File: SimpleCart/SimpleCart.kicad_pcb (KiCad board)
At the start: 2 copper layers, 90 x 56.8 mm, 9 parts, among them J1 CommanderX16Expansion Alt, U1 SST39SF040 (ROM), U2 74HCT00, U3 74HCT138

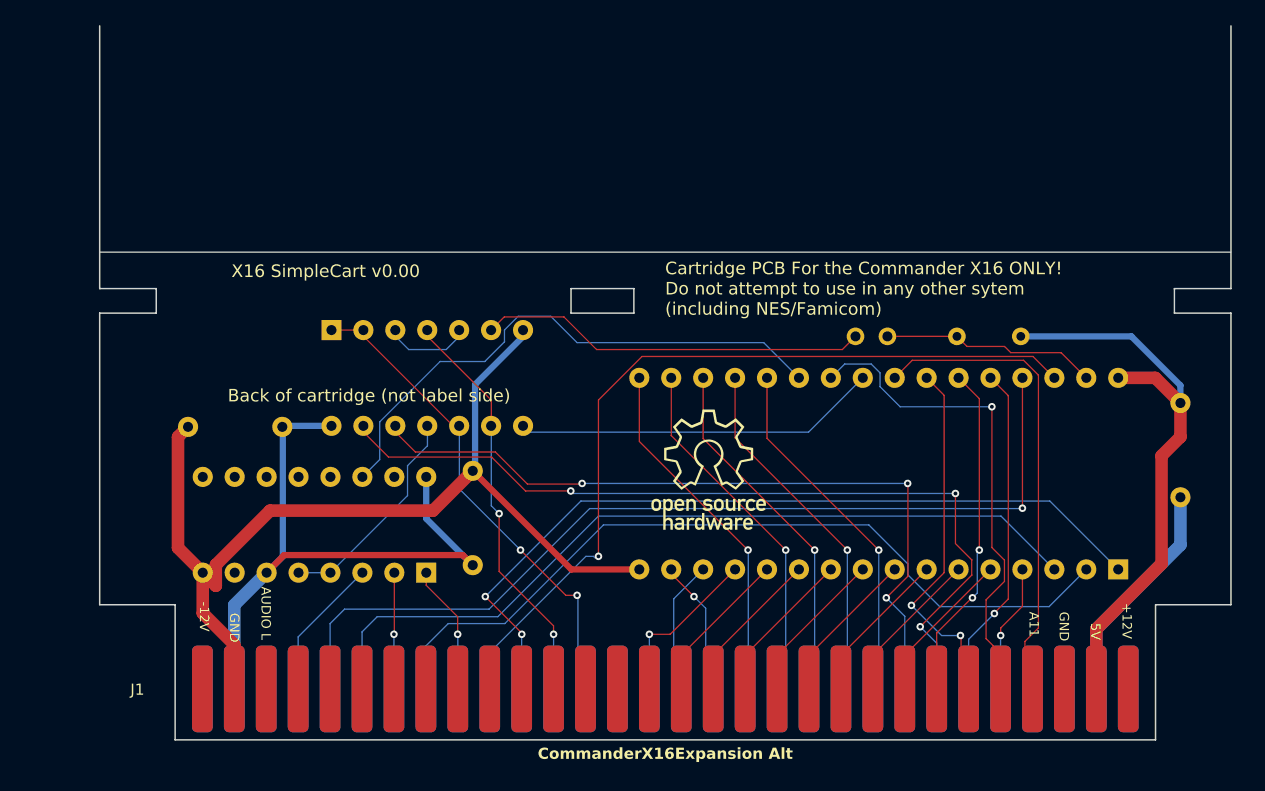
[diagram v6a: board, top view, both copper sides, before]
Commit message: Tweaks to both Simplecart and ROAM
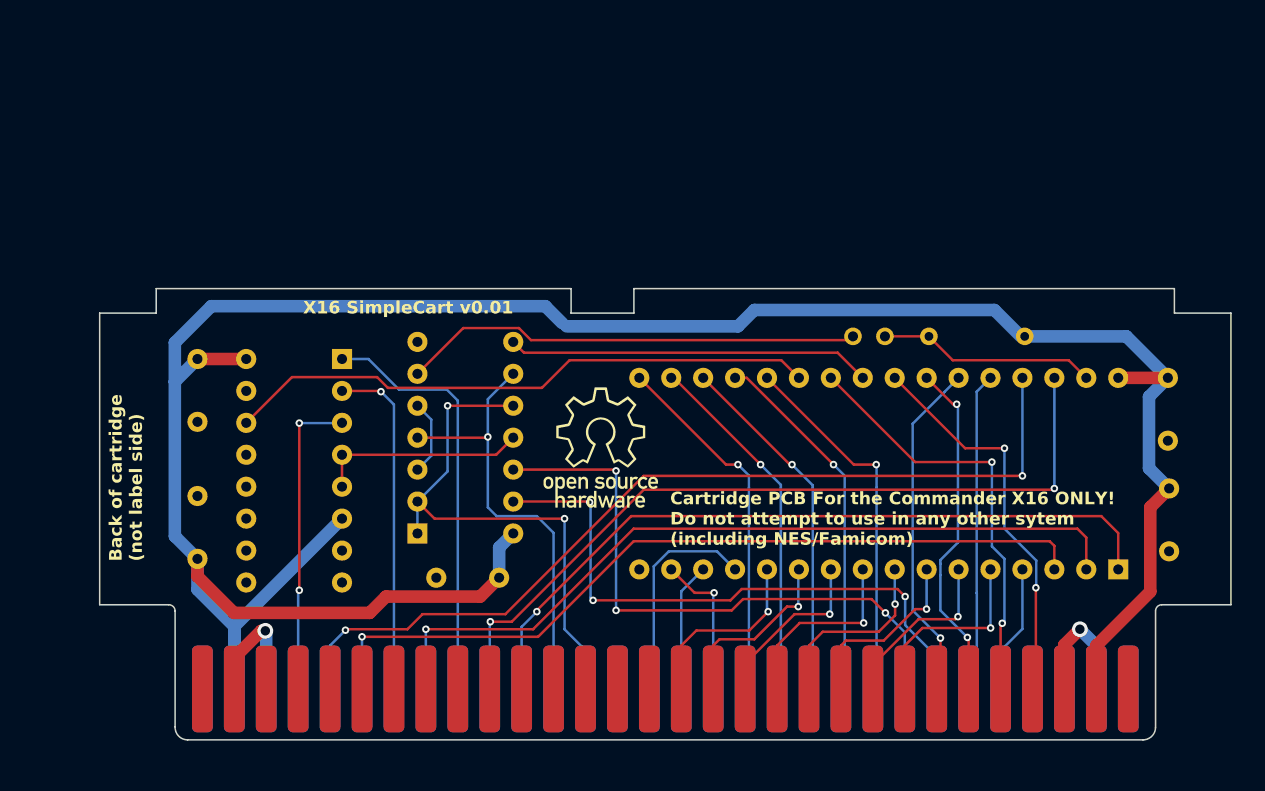
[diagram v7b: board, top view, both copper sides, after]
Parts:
- added C4: 1uF, Capacitor_THT:C_Disc_D4.3mm_W1.9mm_P5.00mm, B.Cu at (133.1, 119.8)
- added C5: 1uF, Capacitor_THT:C_Disc_D4.3mm_W1.9mm_P5.00mm, B.Cu at (55.8, 115.4)
- C1, C2, C3: footprint Capacitor_THT:C_Axial_L3.8mm_D2.6mm_P7.50mm_Horizontal -> Capacitor_THT:C_Disc_D4.3mm_W1.9mm_P5.00mm
- J1: footprint CommanderX16Expansion:CommanderX16Cartridge -> CommanderX16Expansion:CommanderX16SimpleCartridge
- JP1: value WRITE ENABLE -> WRITE EN
- R1: footprint Resistor_THT:R_Axial_DIN0204_L3.6mm_D1.6mm_P5.08mm_Horizontal -> Resistor_THT:R_Axial_DIN0204_L3.6mm_D1.6mm_P7.62mm_Horizontal
- moved U3 18.3 mm to (67.3, 104.5), turned to 180 degrees
- moved U2 17.6 mm to (73.3, 118.4), turned to 0 degrees
- moved C2 8.98 mm to (74.8, 121.9), turned to 0 degrees
- moved C3 8.64 mm to (55.8, 104.5), turned to -90 degrees
- moved C1 4.61 mm to (133.0, 111.0)
- moved R1 2.23 mm to (114.0, 102.7)
- moved JP1 0.20 mm to (108.0, 102.7)
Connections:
- J1 pad 1: Net-(J1--12V-Pad1) -> unconnected-(J1--12V-Pad1)_1
- J1 pad 2: Net-(J1-+12V-Pad2) -> unconnected-(J1-+12V-Pad2)
- J1 pad 59: Net-(J1-+12V-Pad2) -> unconnected-(J1-+12V-Pad2)_1
- J1 pad 60: Net-(J1--12V-Pad1) -> unconnected-(J1--12V-Pad1)
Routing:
- net +5V: track 99.0 -> 200.1 mm
- net GND: track 96.6 -> 21.0 mm, vias 0 -> 2
- net Net-(J1-ROMB5): track 12.9 -> 33.5 mm, vias 1 -> 0
- net Net-(J1-A14): track 67.6 -> 47.9 mm
- net Net-(J1-ROMB6): track 8.66 -> 27.3 mm
- net Net-(J1-ROMB7): track 11.4 -> 24.6 mm, vias 0 -> 2
- net Net-(J1-A15): track 60.2 -> 48.3 mm
- net A11: track 37.9 -> 31.4 mm, vias 0 -> 2
- net !MEMWE: track 30.9 -> 36.6 mm
- net A7: track 12.6 -> 17.5 mm, vias 0 -> 1
- net A10: track 39.0 -> 34.2 mm, vias 1 -> 2
- net A6: track 12.6 -> 17.3 mm, vias 0 -> 1
- net Net-(J1-RWB): track 38.4 -> 42.9 mm
- net D0: track 13.3 -> 17.5 mm, vias 1 -> 0
- net ROMB4: track 63.7 -> 59.6 mm, vias 2 -> 1
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- added copper zone on In1.Cu, net GND
- added copper zone on In2.Cu, net GND
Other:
- board size 90 x 56.8 mm -> 90 x 35.9 mm
- copper layers 2 -> 4
- board text added: "Front of cartridge label side"
- board text added: "X16 SimpleCart v0.01"
- board text removed: "+12V"
- board text removed: "+5V"
- board text removed: "-12V"
- board text removed: "5V"
- board text removed: "A11"
- board text removed: "AUDIO L"
- board text removed: "Front of cartridge, label side"
- board text removed: "GND"
- board text removed: "ROMB7"
- board text removed: "SCL"
- board text removed: "X16 SimpleCart v0.00"

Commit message: Ground vias
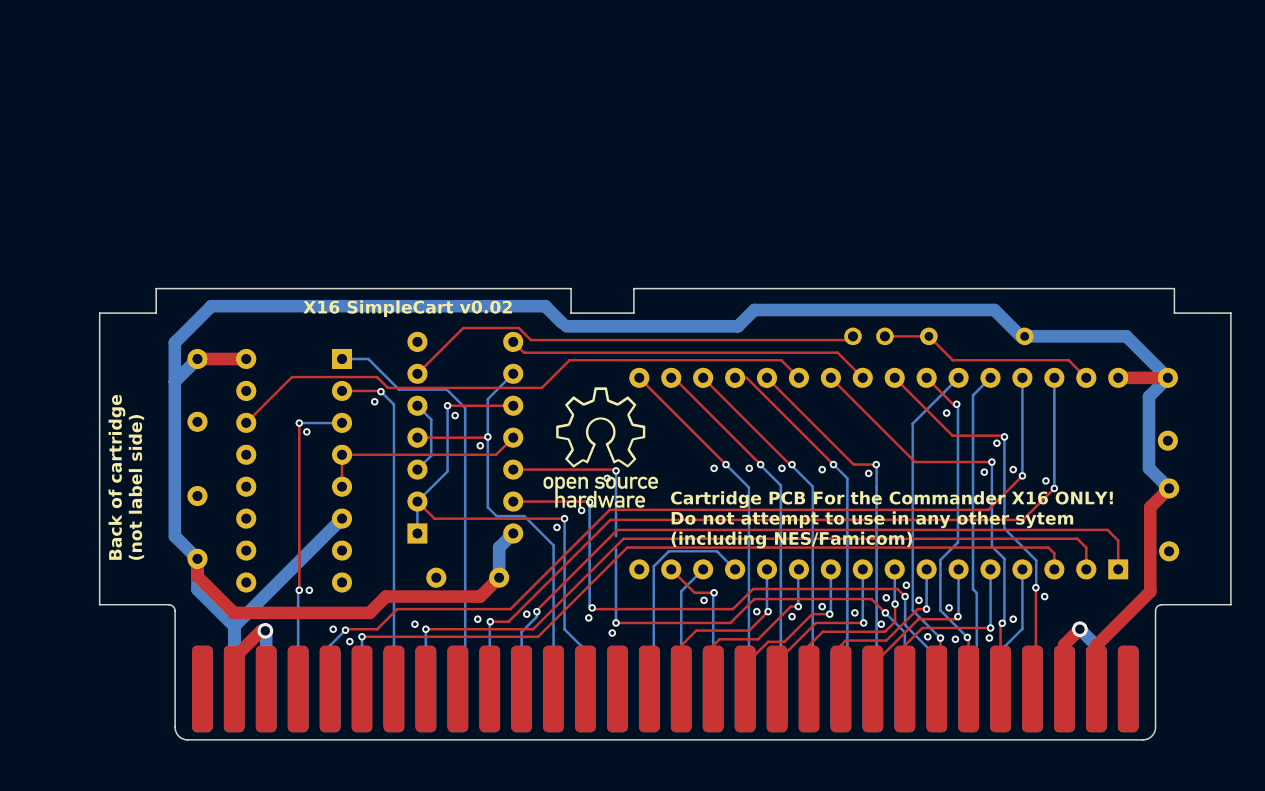
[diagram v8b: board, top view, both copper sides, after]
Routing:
- net ROMB4: track 59.6 -> 58.4 mm
- net ROMB2: track 63.6 -> 62.5 mm
- net Net-(J1-A14): track 47.9 -> 48.9 mm
- net ROMB1: track 64.4 -> 63.6 mm
- net A3: track 15.4 -> 14.6 mm
- net Net-(J1-PHI2): track 35.6 -> 35.0 mm
- net D3: track 29.0 -> 28.5 mm
- net A11: track 31.4 -> 31.9 mm
- net GND: vias 2 -> 42
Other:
- board text added: "X16 SimpleCart v0.02"
- board text removed: "X16 SimpleCart v0.01"
